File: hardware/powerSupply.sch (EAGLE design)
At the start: 94 parts, among them IC1 MCP3008, IC12 LM358, IC13 LM358, IC2 LM334Z, IC3 MCP4821P, IC4 MCP4821P, IC5 74LS139D, IC6 7805TV, IC7 LP2950Z, IC8 LT3080T, IC9 MAX874CPA, J3 RASPBERRYPI-40-PIN-GPIO_PTH, SW1 EC11B_SW, SW2 EC11B_SW, SW7 B3F-1000, T1 2N3904, T2 2N3904

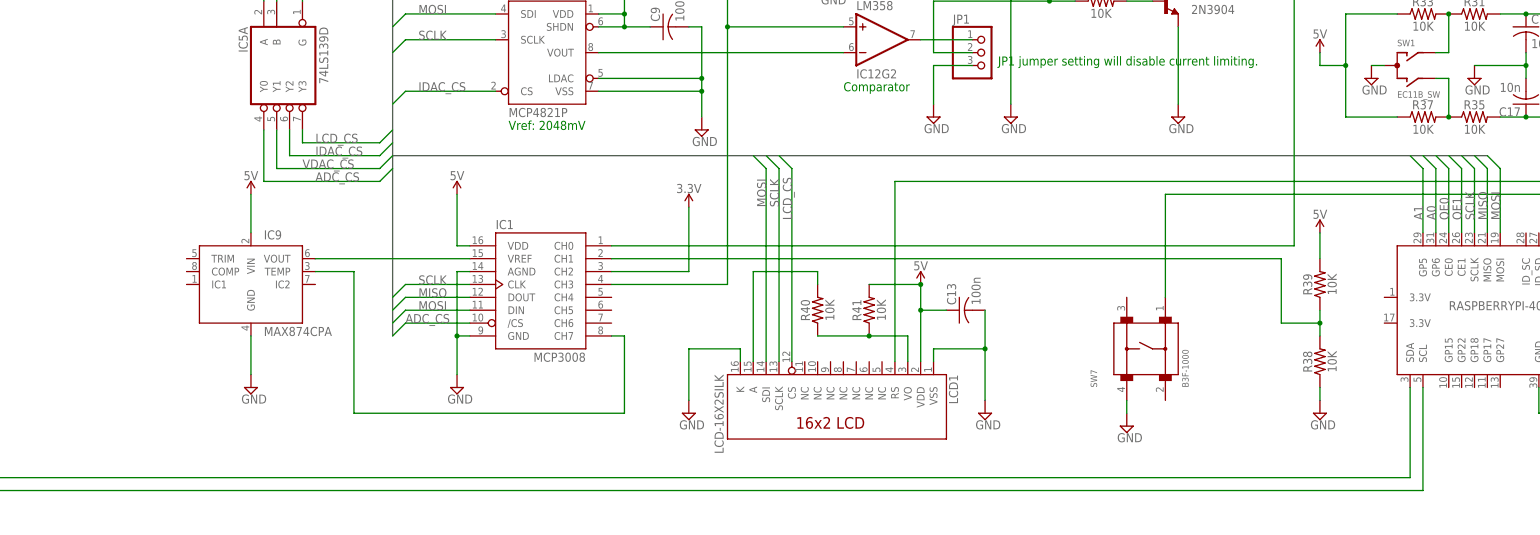
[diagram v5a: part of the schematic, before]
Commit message: added the trimmers. and LCD switch tranny
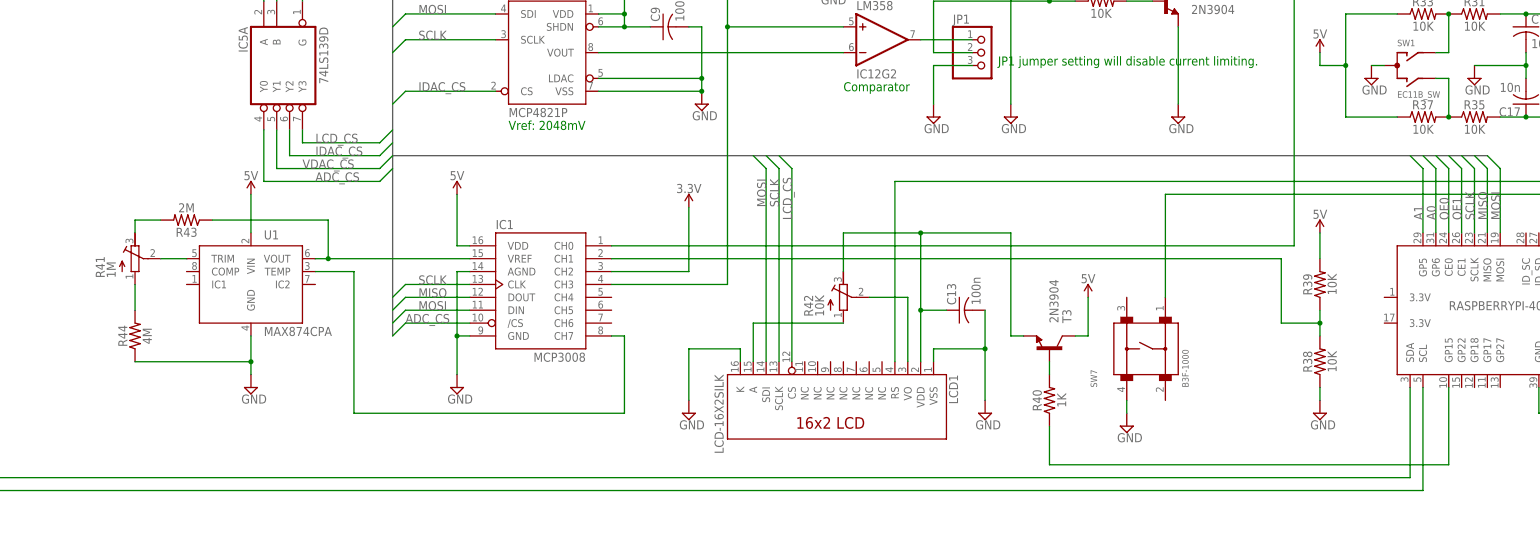
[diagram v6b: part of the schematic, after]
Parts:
- removed IC9: MAX874CPA, mixedSignal:MAX874CPA
- added R42: 10K, resistor:R-TRIMM64W
- added R43: 2M, rcl:R-US_0204/7
- added R44: 4M, rcl:R-US_0204/7
- added T3: 2N3904, transistor:2N3904
- added U1: MAX874CPA, Hexellence-mixedSignal:MAX874CPA
- R40: value 10K -> 1K
- R41: value 10K -> 1M; device rcl:R-US_0204/7 -> resistor:R-TRIMM64W
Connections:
- new net N$37: R40.2, T3.B
- new net N$38: C13.1, LCD1.VDD, R42.E, T3.E
- new net N$39: J3.GP15, R40.1
- new net N$40: R41.S, U1.TRIM
- new net N$41: R41.E, R43.2
- new net N$43: R41.A, R44.2
- net 4.096V: now also R43.1, U1.VOUT; no longer IC9.VOUT
- net 5V: now also T3.C, U1.VIN; no longer C13.1, IC9.VIN, LCD1.VDD, R41.2
- net GND: now also R44.1, U1.GND; no longer IC9.GND
- net N$18: now also R42.A; no longer R40.2
- net N$3: now also R42.S; no longer R40.1, R41.1
- net N$5: now also U1.TEMP; no longer IC9.TEMP
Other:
- moved on the sheet: R40

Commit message: 
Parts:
- removed J5, J6, J7: (no value), Hexellence-Connectors:CONN_022.54MM_SCREWTERM
- added R45, R46: Don't populate, rcl:R-US_0204/7
- added X1: VOUT, con-wago-500:W237-102
- added X2: VSENSE, con-wago-500:W237-102
- added X3: VIN, con-wago-500:W237-102
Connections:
- new net N$42: J3.3.3V@1, J3.3.3V@17, R45.2
- new net N$44: J3.5V@2, J3.5V@4, R46.2
- net 3.3V: now also R45.1
- net 5V: now also R46.1
- net GND: now also X1-2.KL, X2-2.KL, X3-2.KL; no longer J5.2, J6.2, J7.2
- net V+: now also X3-1.KL; no longer J5.1
- net VOUT: now also X1-1.KL; no longer J6.1
- net VSENS: now also X2-1.KL; no longer J7.1
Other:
- moved on the sheet: R38, R39

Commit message: 
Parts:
- removed ICG3: LM358, SparkFun-IC-Amplifiers:LM358
- removed LED1: (no value), led:LED5MM
- removed R24: 470R, rcl:R-US_0204/7
- removed R46: Don't populate, rcl:R-US_0204/7
- removed SW3, SW4, SW5, SW6: (no value), adafruit:SWITCH_PUSHBUTTONEVQ-PE
- removed T2: 2N3904, transistor:2N3904
- added C12, C24: 100n, adafruit:C-US050-024X044
- added JP2: (no value), pinhead:PINHD-1X5
- R23, R32: value 10K -> 10R; device rcl:R-US_0204/7 -> adafruit:R-US_0207/12
- R28, R29: value 10R -> 10K
- R33: device rcl:R-US_0204/7 -> resistor:R-TRIMM64W
- R42: value 10K -> 2M; device resistor:R-TRIMM64W -> rcl:R-US_0204/7
- R43: value 2M -> 4M
- R44: value 4M -> Don't populate
- renumbered IC13 to IC9
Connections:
- removed net N$15: R23.2, T2.B
- removed net N$16: LED1.C, T2.C
- removed net N$17: LED1.A, R24.1
- net 3.3V: now also R44.1; no longer R45.1
- net 4.096V: now also R42.1; no longer R43.1
- net 5V: now also C12.1, C24.1, R30.1, R31.1, R45.1; no longer R24.2, R32.1, R33.1, R46.1
- net GND: now also C12.2, C24.2, IC9G3.P$V-, JP2.5, R43.1; no longer ICG3G3.P$V-, R44.1, SW3.P$2, SW4.P$2, SW5.P$2, SW6.P$2, T2.E
- net N$18: now also R33.A; no longer R42.A
- net N$19: now also R32.1; no longer R28.2
- net N$20: now also J3.GP22; no longer R23.1
- net N$22: now also R28.1, R30.2; no longer R30.1, R32.2
- net N$23: now also R28.2; no longer R30.2
- net N$26: now also R29.2; no longer R31.2
- net N$28: now also R29.1, R31.2; no longer R31.1, R33.2
- net N$3: now also R33.S; no longer R42.S
- net N$30: now also JP2.1; no longer SW3.P$1
- net N$31: now also JP2.2; no longer SW4.P$1
- net N$32: now also JP2.3; no longer SW5.P$1
- net N$33: now also JP2.4; no longer SW6.P$1
- net N$38: now also R33.E; no longer R42.E
- net N$4: now also R23.1; no longer R29.1
- net N$41: now also R42.2; no longer R43.2
- net N$42: now also R44.2; no longer R45.2
- net N$43: now also R43.2; no longer R44.2
- net N$44: now also R45.2; no longer R46.2
- net V+: now also R23.2; no longer R29.2
- net V+1: now also IC9G3.P$V+, R32.2; no longer ICG3G3.P$V+, R28.1
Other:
- note removed: "CLIM LED"
- moved on the sheet: R23, R28, R29, R30, R31, R32, R43, R44, R45
